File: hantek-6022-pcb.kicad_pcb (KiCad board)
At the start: 2 copper layers, 31.8 x 19 mm, 15 parts, among them J1 R17, J2 BNC_A, J3 BNC_B, J4 R27, J5 AC_B, J6 AC_A, J7 GND, U1 TLP175A, U2 TLP175A

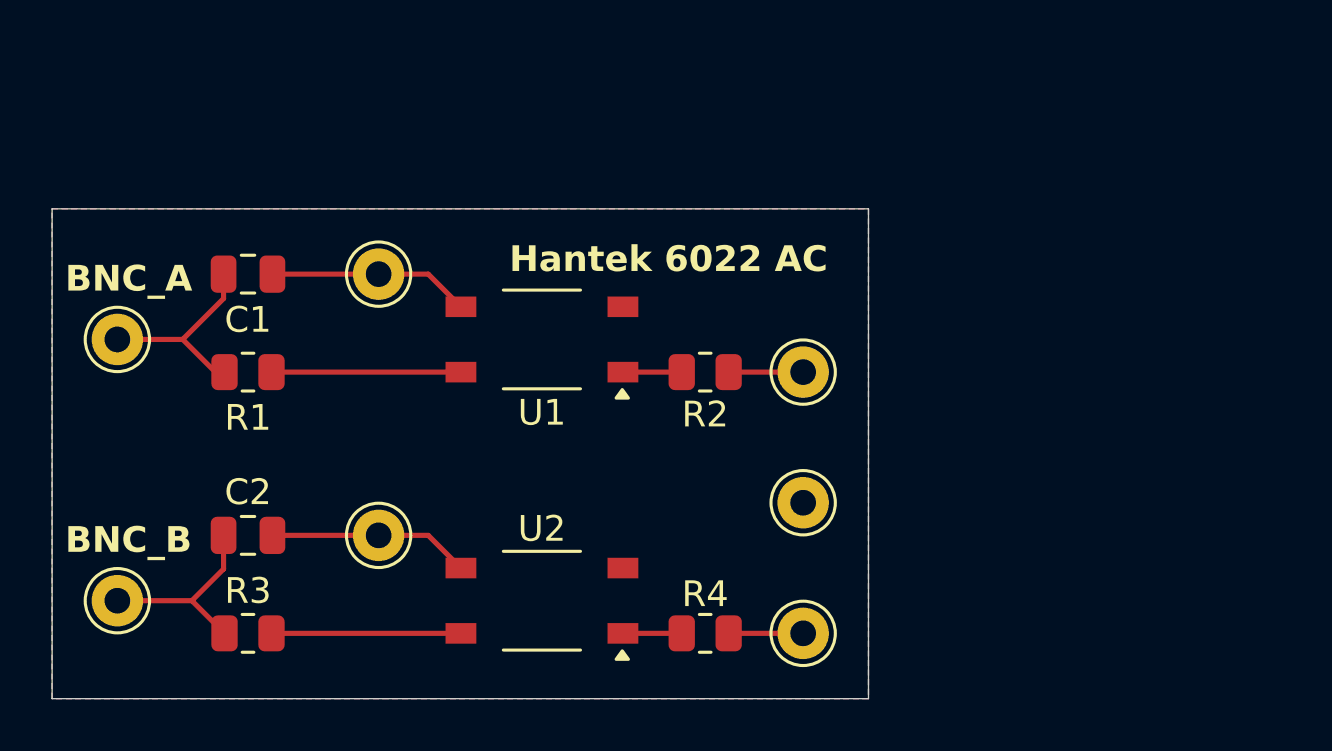
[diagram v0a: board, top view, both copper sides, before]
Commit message: reduce pcb size, add readme
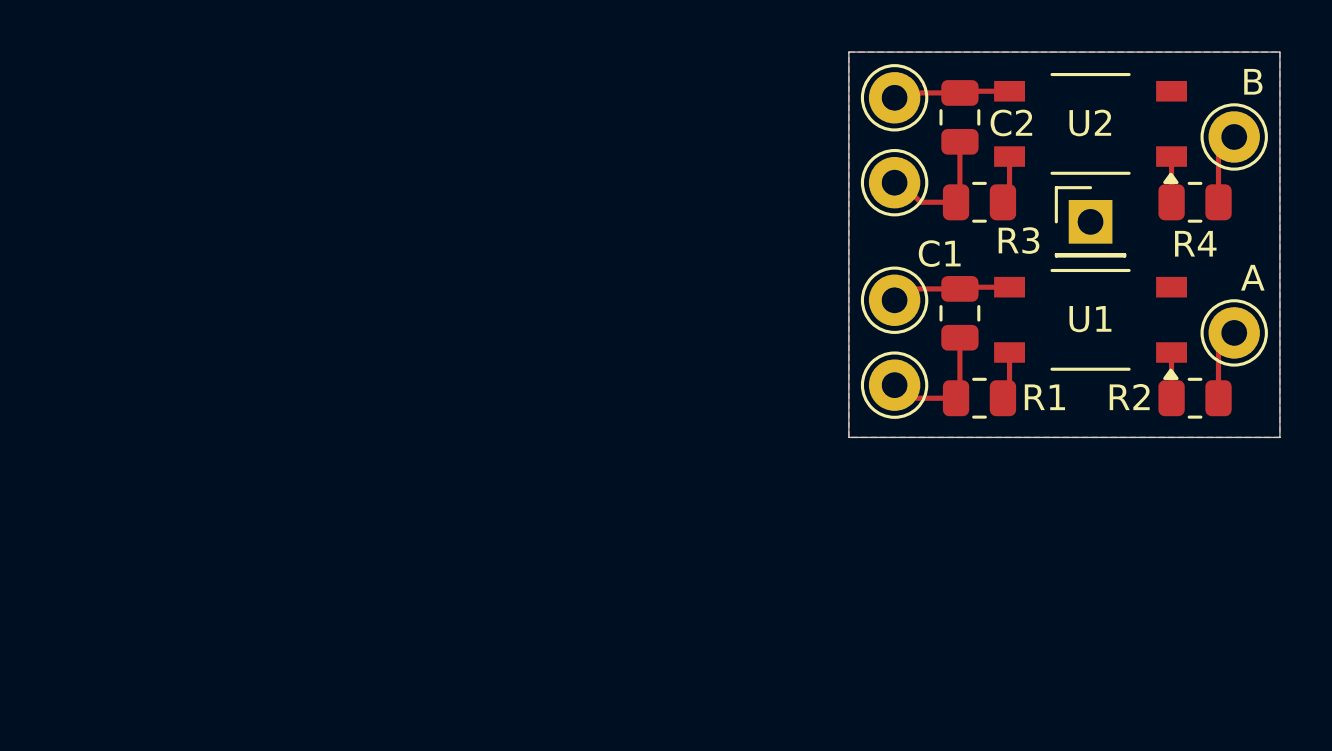
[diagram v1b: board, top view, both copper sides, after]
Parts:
- J7: value GND -> Conn_01x01; footprint Connector_Pin:Pin_D1.0mm_L10.0mm -> Connector_PinHeader_2.54mm:PinHeader_1x01_P2.54mm_Vertical
- moved J3 34.3 mm to (121.7, 63.8), turned to 180 degrees
- moved R3 33.0 mm to (125.0, 64.5)
- moved C2 32.1 mm to (124.2, 61.2), turned to 90 degrees
- moved J2 30.3 mm to (121.7, 71.6), turned to 180 degrees
- moved R1 28.5 mm to (125.0, 72.1)
- moved U2 28.3 mm to (129.3, 61.5)
- moved C1 27.7 mm to (124.2, 68.8), turned to 90 degrees
- moved J4 26.3 mm to (121.7, 60.5), turned to 180 degrees
- moved J5 25.6 mm to (134.9, 62.0), turned to 180 degrees
- moved R4 25.4 mm to (133.3, 64.5)
- moved U1 21.3 mm to (129.3, 69.1)
- moved J1 20.1 mm to (121.7, 68.3), turned to 180 degrees
- moved R2 19.1 mm to (133.3, 72.1)
- moved J6 16.8 mm to (134.9, 69.6), turned to 180 degrees
- moved J7 15.6 mm to (129.3, 65.3)
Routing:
- net Net-(R1-Pad2): track 7.37 -> 1.88 mm
- net Net-(R3-Pad2): track 7.37 -> 1.88 mm
- net /R27: track 7.86 -> 4.58 mm
- net /R17: track 7.86 -> 4.68 mm
- net /BNC_A: track 7.89 -> 5.01 mm
- net /BNC_B: track 7.74 -> 5.12 mm
- net Net-(R2-Pad2): track 2.29 -> 1.78 mm
- net Net-(R4-Pad2): track 2.29 -> 1.78 mm
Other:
- board size 31.8 x 19 mm -> 16.8 x 15 mm
- board text added: "A"
- board text added: "B"
- board text added: "Ch A"
- board text added: "Ch B"
- board text added: "R17"
- board text added: "R27"
- board text removed: "Hantek 6022 AC"
